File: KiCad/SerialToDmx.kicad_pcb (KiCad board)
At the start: 2 copper layers, 65 x 40 mm, 28 parts, among them U1 XIAO ESP32 C3, U2 TEA1-0505, U3 H11L1, U4 H11L1, U5 H11L1, U6 ST485EBDR, U7 H11L1

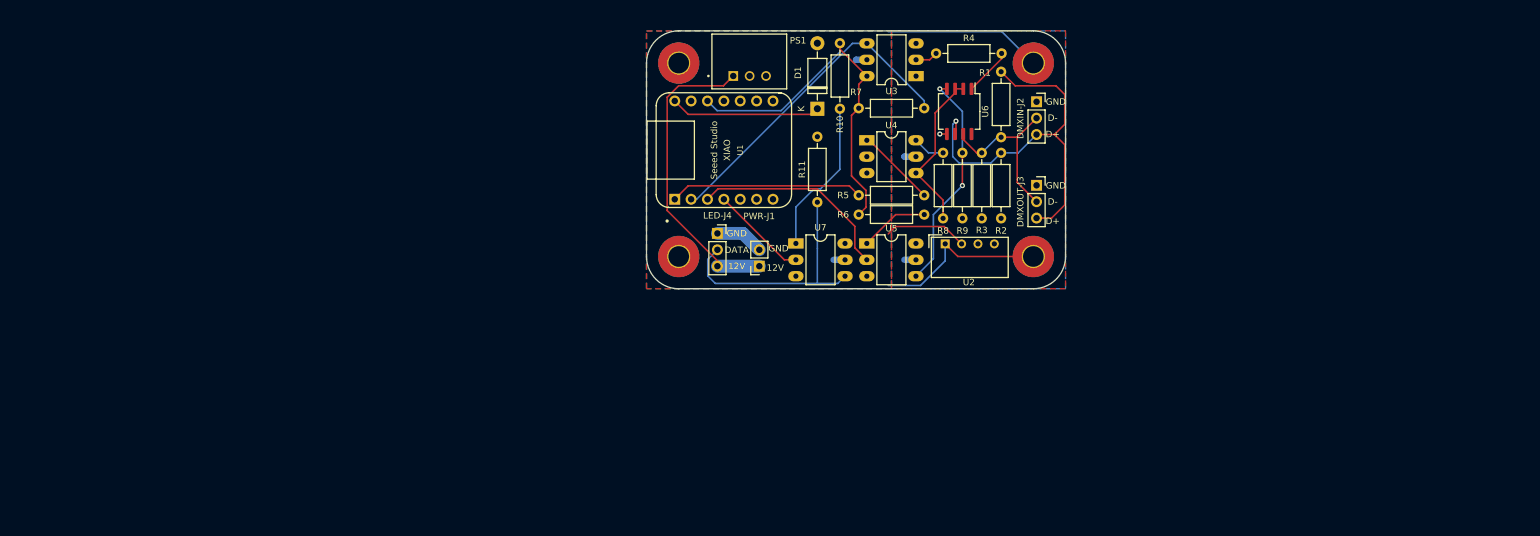
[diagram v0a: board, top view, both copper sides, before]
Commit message: Started Work on Conn Box V2
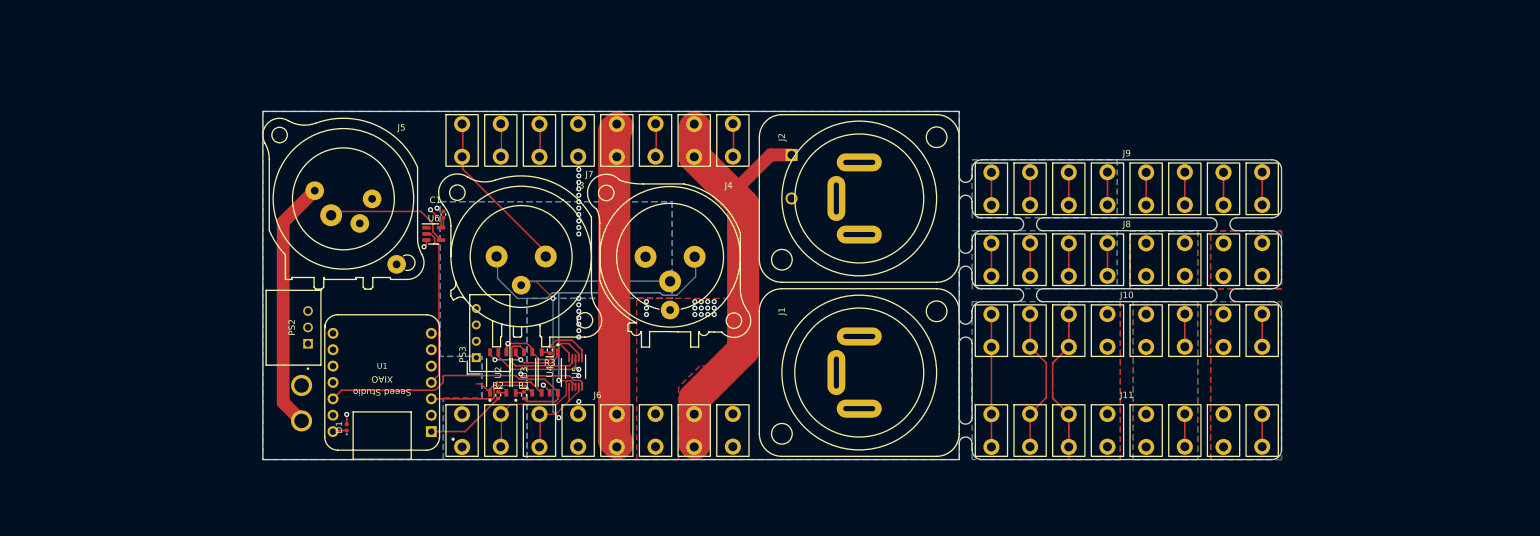
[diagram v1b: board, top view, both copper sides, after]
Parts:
- removed DMXIN-J2, DMXOUT-J3, LED-J4: Conn_01x03_Socket, Connector_PinSocket_2.54mm:PinSocket_1x03_P2.54mm_Vertical
- removed H1, H2, H3, H4: MountingHole_Pad, MountingHole:MountingHole_3.2mm_M3_Pad_TopBottom
- removed PWR-J1: Conn_01x02_Socket, Connector_PinSocket_2.54mm:PinSocket_1x02_P2.54mm_Vertical
- removed R10, R5, R6: 330R, Resistor_THT:R_Axial_DIN0207_L6.3mm_D2.5mm_P10.16mm_Horizontal
- removed R11, R4, R7, R8, R9: 470R, Resistor_THT:R_Axial_DIN0207_L6.3mm_D2.5mm_P10.16mm_Horizontal
- removed U7: H11L1, Package_DIP:DIP-6_W7.62mm_LongPads
- added C1: 0.1uC, Capacitor_SMD:C_0402_1005Metric, F.Cu at (118.5, 81.0)
- added J1: NAC3MPXXA, NeutrikCustom:NAC3MPXXA, F.Cu at (183.0, 105.5)
- added J10: Conn_01x08_Pin, Connector_Faston_Custom:Faston_01x08_pin, F.Cu at (203.5, 99.0)
- added J11: Conn_01x08_Pin, Connector_Faston_Custom:Faston_01x08_pin, F.Cu at (203.5, 114.5)
- added J2: NAC3MPXXB, NeutrikCustom:NAC3MPXXB, F.Cu at (183.0, 78.5)
- added J3: NC3FAV, NeutrikCustom:NC3FAV, F.Cu at (130.8, 86.5)
- added J4: NC3MAV, NeutrikCustom:NC3MAV, F.Cu at (153.8, 86.5)
- added J5: NC4FAV, NeutrikCustom:NC4FAV, F.Cu at (103.0, 77.5)
- added J6: Conn_01x08_Socket, Connector_Faston_Custom:Faston_01x08_socket, F.Cu at (121.4, 114.5)
- added J7: Conn_01x08_Socket, Connector_Faston_Custom:Faston_01x08_socket, F.Cu at (121.4, 69.5)
- added J8: Conn_01x08_Pin, Connector_Faston_Custom:Faston_01x08_pin, F.Cu at (203.5, 88.0)
- added J9: Conn_01x08_Pin, Connector_Faston_Custom:Faston_01x08_pin, F.Cu at (203.5, 77.0)
- added PS2: R-78E5.0-0.5, CONV_R-78E5.0-0.5:CONV_R-78E5.0-0.5, F.Cu at (95.2, 98.5)
- added PS3: TEA1-0505, Converter_DCDC:Converter_DCDC_TRACO_TEA1-xxxx_THT, F.Cu at (123.6, 103.2)
- D1: footprint Diode_THT:D_DO-41_SOD81_P10.16mm_Horizontal -> Diode_SMD:D_0402_1005Metric
- PS1: value R-78E5.0-0.5 -> IRM-45-12; footprint CONV_R-78E5.0-0.5:CONV_R-78E5.0-0.5 -> IRM-45-12:CONV_IRM-45-12; moved to B.Cu
- R1: value 120R -> 169R; footprint Resistor_THT:R_Axial_DIN0207_L6.3mm_D2.5mm_P10.16mm_Horizontal -> Resistor_SMD:R_0402_1005Metric
- R2: value 720R -> 169R; footprint Resistor_THT:R_Axial_DIN0207_L6.3mm_D2.5mm_P10.16mm_Horizontal -> Resistor_SMD:R_0402_1005Metric
- R3: value 720R -> 330R; footprint Resistor_THT:R_Axial_DIN0207_L6.3mm_D2.5mm_P10.16mm_Horizontal -> Resistor_SMD:R_0402_1005Metric
- U2: value TEA1-0505 -> ISOM8710DFFR; footprint Converter_DCDC:Converter_DCDC_TRACO_TEA1-xxxx_THT -> TICustom:ISOM8710
- U3, U4: value H11L1 -> ISOM8710DFFR; footprint Package_DIP:DIP-6_W7.62mm_LongPads -> TICustom:ISOM8710
- U5: value H11L1 -> THVD1512DGS; footprint Package_DIP:DIP-6_W7.62mm_LongPads -> TICustom:DGS0010A_N
- U6: value ST485EBDR -> SN74LV1T34DBV; footprint Package_SO:SO-8_5.3x6.2mm_P1.27mm -> Package_TO_SOT_SMD:SOT-23-5
- moved D1 88.2 mm to (103.5, 114.0)
- moved R1 84.1 mm to (131.0, 109.0)
- moved U6 83.7 mm to (117.0, 84.0), turned to 0 degrees
- moved R2 82.7 mm to (127.0, 109.0)
- moved U3 76.2 mm to (131.0, 105.5), turned to 90 degrees
- moved R3 73.6 mm to (135.0, 102.0), turned to 90 degrees
- moved U2 72.1 mm to (127.0, 105.5), turned to 90 degrees
- moved U1 64.1 mm to (109.0, 107.0), turned to 180 degrees
- moved U4 61.0 mm to (135.0, 105.5), turned to -90 degrees
- moved U5 49.4 mm to (139.0, 105.5), turned to -90 degrees
- moved PS1 47.6 mm to (134.3, 92.8), turned to 180 degrees
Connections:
- R1 pad 1: Net-(DMXIN-J2-Pin_2) -> 3V3
- R1 pad 2: Net-(DMXIN-J2-Pin_3) -> Net-(U3-AN)
- R2 pad 1: VCC_Iso -> DMX_DRIVE
- R2 pad 2: Net-(DMXIN-J2-Pin_3) -> Net-(U2-CAT)
- R3 pad 1: Net-(DMXIN-J2-Pin_2) -> Net-(U4-CAT)
- R3 pad 2: GND_Iso -> Net-(U5-R)
- U1 pad 1: DMX_READ -> DMX_DRIVE
- U1 pad 4: LED_DATA -> LED_DATA_33
- U2 pad 2: 5V -> Net-(U2-CAT)
- U2 pad 4: VCC_Iso -> Net-(U2-OUT)
- U3 pad 1: VCC_Iso -> Net-(U3-AN)
- U3 pad 2: Net-(R4-Pad1) -> DMX_TX
- U3 pad 3: unconnected-(U3-Pad3) -> GND_Iso
- U3 pad 4: DMX_RX -> Net-(U3-OUT)
- U3 pad 5: GND -> VCC_Iso
- U4 pad 1: Net-(R5-Pad2) -> VCC_Iso
- U4 pad 2: GND -> Net-(U4-CAT)
- U4 pad 3: unconnected-(U4-Pad3) -> GND
- U4 pad 4: Net-(U6-DE) -> DMX_RX
- U4 pad 5: GND_Iso -> 3V3
- U5 pad 1: Net-(R6-Pad2) -> Net-(U5-R)
- U5 pad 2: DMX_TX -> GND_Iso
- U5 pad 3: unconnected-(U5-Pad3) -> Net-(U2-OUT)
- U5 pad 4: Net-(U6-DI) -> Net-(U3-OUT)
- U5 pad 6: VCC_Iso -> DMX+
- U6 pad 1: Net-(U6-RO) -> unconnected-(U6-NC-Pad1)
- U6 pad 2: Net-(U6-DE) -> LED_DATA_33
- U6 pad 3: Net-(U6-DE) -> GND
- U6 pad 4: Net-(U6-DI) -> LED_DATA_50
- U6 pad 5: GND_Iso -> 5V
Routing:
- net N: track 0.00 -> 128.5 mm
- net L: track 0.00 -> 122.2 mm
- net DMX-: track 0.00 -> 97.5 mm, vias 0 -> 1
- net DMX+: track 0.00 -> 89.6 mm, vias 0 -> 2
- net Net-(DMXIN-J2-Pin_3): track 60.6 -> 0.00 mm, vias 1 -> 0
- net GND: track 63.1 -> 112.8 mm, vias 0 -> 23
- net GND_Iso: track 4.69 -> 46.4 mm
- net Net-(LED-J4-Pin_2): track 39.5 -> 0.00 mm
- net Net-(U6-DI): track 34.6 -> 0.00 mm, vias 2 -> 0
- net 12V: track 47.6 -> 81.9 mm
- net DMX_RX: track 51.0 -> 20.9 mm, vias 0 -> 1
- net DMX_READ: track 30.0 -> 0.00 mm
- net Net-(DMXIN-J2-Pin_2): track 26.0 -> 0.00 mm
- net Net-(U6-DE): track 25.0 -> 0.00 mm
- net LED_DATA_33: track 0.00 -> 24.8 mm
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- added copper zone on In2.Cu, net 5V
- added copper zone on B.Cu, net GND-Connection-Bridge
- added copper zone on F.Cu, net GND-Connection-Bridge
- added copper zone on In1.Cu, net GND-Connection-Bridge
- added copper zone on In2.Cu, net GND-Connection-Bridge
- added copper zone on B.Cu, net GND-Connection-In-Termination
- added copper zone on In1.Cu, net GND-Connection-In-Termination
- added copper zone on In2.Cu, net GND-Connection-In-Termination
- added copper zone on B.Cu, net GND-Connection-Out-Termination
- added copper zone on In1.Cu, net GND-Connection-Out-Termination
- added copper zone on In2.Cu, net GND-Connection-Out-Termination
- added copper zone on B.Cu, net L-Connection-Bridge
- added copper zone on F.Cu, net L-Connection-Bridge
- added copper zone on In1.Cu, net L-Connection-Bridge
- added copper zone on In2.Cu, net L-Connection-Bridge
- added copper zone on B.Cu, net L-Connection-Termination
- added copper zone on F.Cu, net L-Connection-Termination
- added copper zone on In1.Cu, net L-Connection-Termination
- added copper zone on In2.Cu, net L-Connection-Termination
- added copper zone on In2.Cu, net L-switched
- added copper zone on B.Cu, net N-Connection-Bridge
- added copper zone on F.Cu, net N-Connection-Bridge
- added copper zone on In1.Cu, net N-Connection-Bridge
- added copper zone on In2.Cu, net N-Connection-Bridge
- added copper zone on B.Cu, net N-Connection-Termination
- added copper zone on F.Cu, net N-Connection-Termination
- added copper zone on In1.Cu, net N-Connection-Termination
- added copper zone on In2.Cu, net N-Connection-Termination
- added copper zone on F.Cu, net N-switched
- added copper zone on In1.Cu, net N-switched
- added copper zone on In2.Cu, net N-switched
- added copper zone on In2.Cu, net VCC_Iso
- removed copper zone on F.Cu, net 5V
- removed copper zone on F.Cu, net VCC_Iso
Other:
- board size 65 x 40 mm -> 158 x 54 mm
- copper layers 2 -> 4

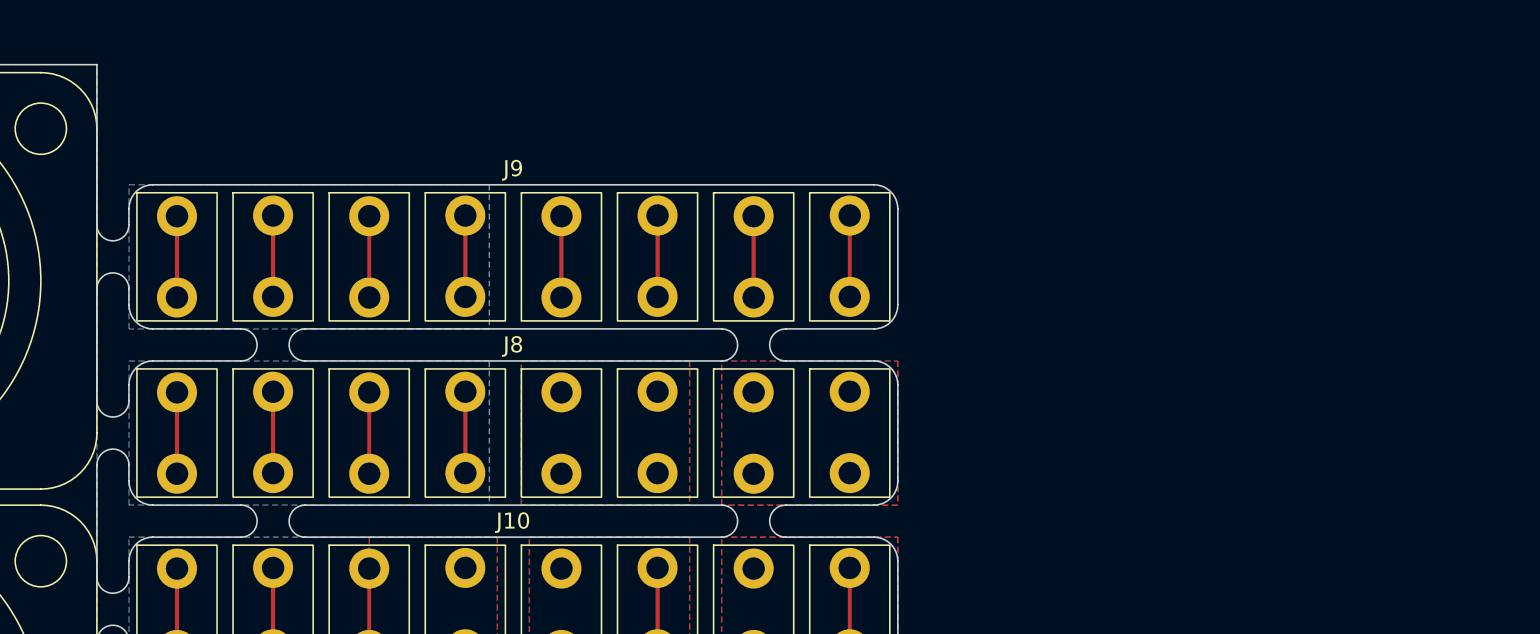
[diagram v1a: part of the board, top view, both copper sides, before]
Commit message: Started on Mounting Holes for Terminators and Bridge
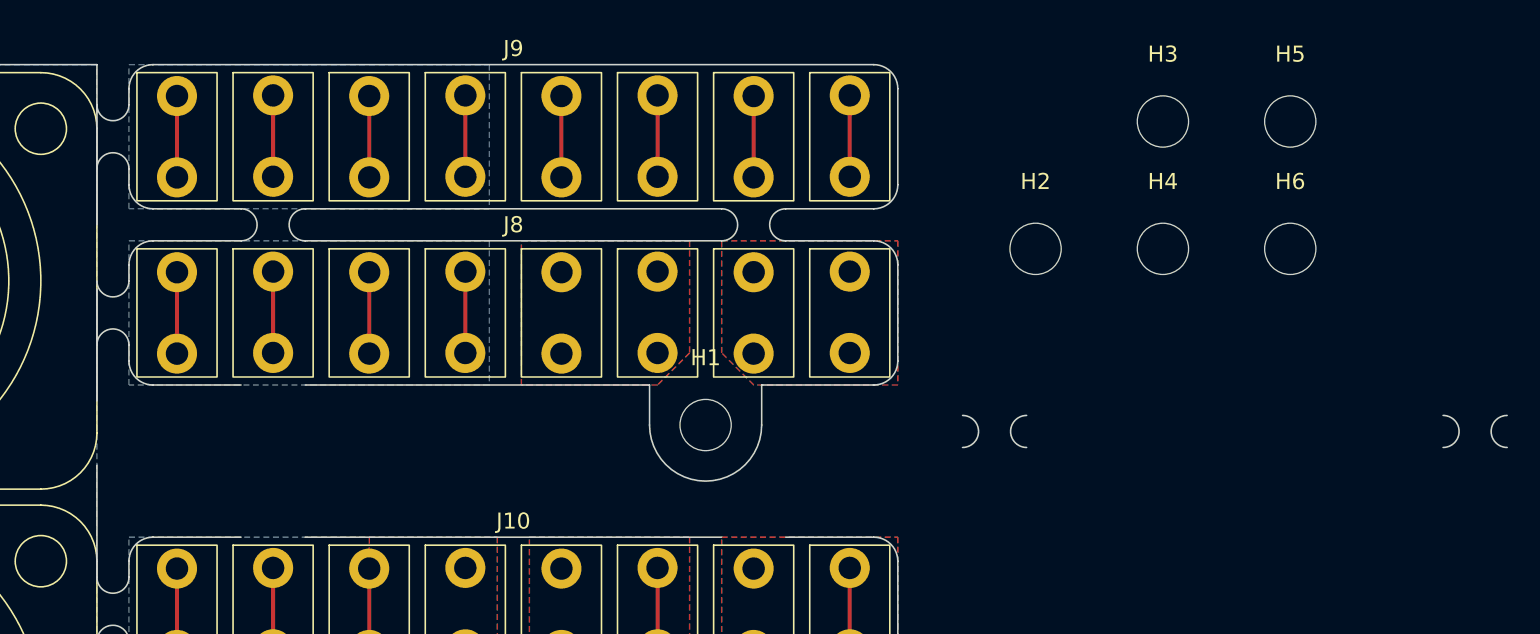
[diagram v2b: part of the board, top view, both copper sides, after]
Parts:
- added H1: MountingHole, MountingHole:MountingHole_3.2mm_M3, F.Cu at (236.5, 87.5)
- added H2: MountingHole, MountingHole:MountingHole_3.2mm_M3, F.Cu at (257.1, 76.5)
- added H3: MountingHole, MountingHole:MountingHole_3.2mm_M3, F.Cu at (265.1, 68.5)
- added H4: MountingHole, MountingHole:MountingHole_3.2mm_M3, F.Cu at (265.1, 76.5)
- added H5: MountingHole, MountingHole:MountingHole_3.2mm_M3, F.Cu at (273.0, 68.5)
- added H6: MountingHole, MountingHole:MountingHole_3.2mm_M3, F.Cu at (273.0, 76.5)
- moved J8 7.50 mm to (203.5, 80.5)
- moved J9 7.50 mm to (203.5, 69.5)
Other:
- board size 158 x 54 mm -> 196 x 54 mm

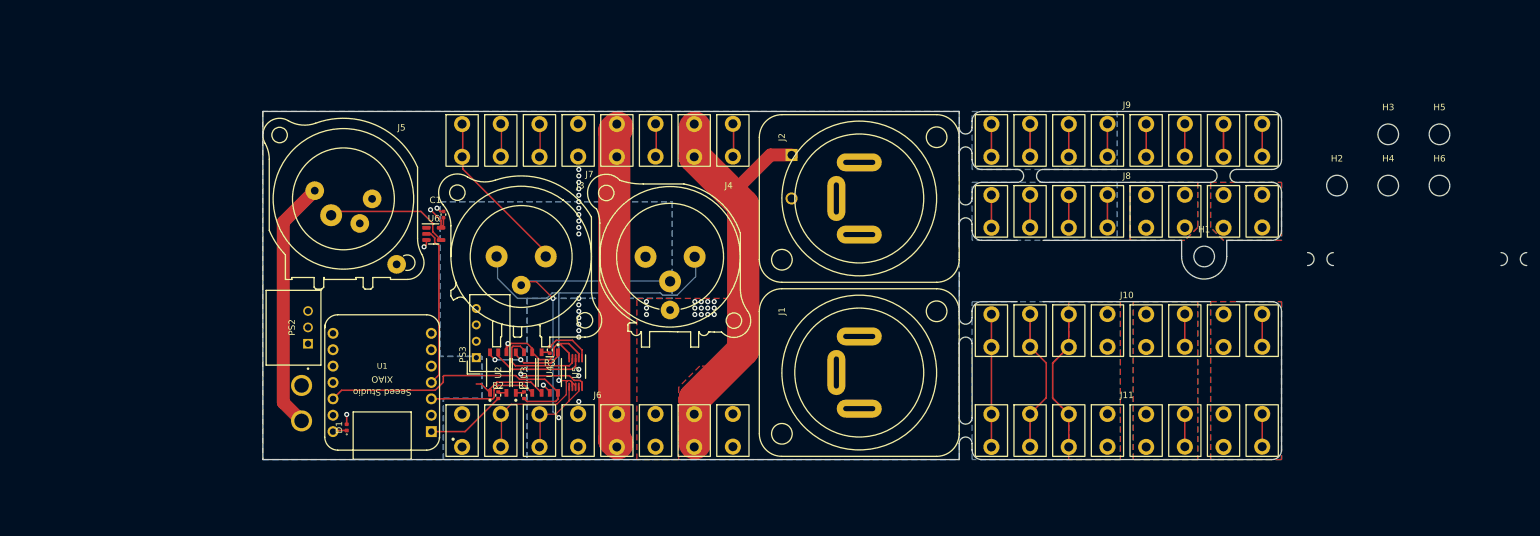
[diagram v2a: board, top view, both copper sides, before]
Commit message: Improved Layout for Case
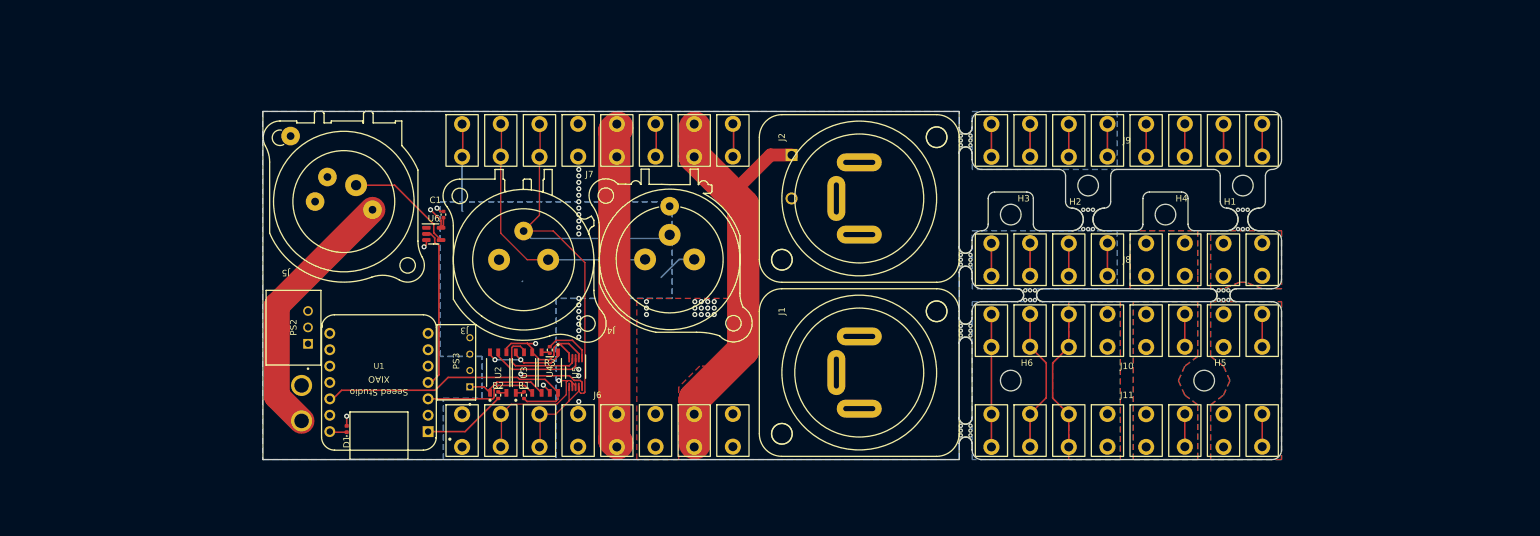
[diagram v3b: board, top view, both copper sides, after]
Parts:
- added H10: Mousebite, Panelization:mouse-bite-2mm-slot, F.Cu at (199.5, 88.0)
- added H11: Mousebite, Panelization:mouse-bite-2mm-slot, F.Cu at (199.5, 69.5)
- added H12: Mousebite, Panelization:mouse-bite-3.5mm-slot, F.Cu at (218.5, 81.8)
- added H13: Mousebite, Panelization:mouse-bite-3.5mm-slot, F.Cu at (242.5, 81.8)
- added H14: Mousebite, Panelization:mouse-bite-2mm-slot, F.Cu at (199.5, 114.5)
- added H7: Mousebite, Panelization:mouse-bite-2mm-slot, F.Cu at (239.5, 93.5)
- added H8: Mousebite, Panelization:mouse-bite-2mm-slot, F.Cu at (209.5, 93.5)
- added H9: Mousebite, Panelization:mouse-bite-2mm-slot, F.Cu at (199.5, 99.0)
- PS3: footprint Converter_DCDC:Converter_DCDC_TRACO_TEA1-xxxx_THT -> TracoCustom:CONV_TEA_1-0505
- moved H6 73.1 mm to (206.5, 106.8)
- moved H3 59.9 mm to (206.5, 81.0)
- moved H5 52.8 mm to (236.5, 106.8)
- moved H2 38.6 mm to (218.5, 76.5)
- moved H4 34.8 mm to (230.5, 81.0)
- moved H1 12.5 mm to (242.5, 76.5)
- moved J8 7.50 mm to (203.5, 88.0)
- moved J5 2.54 mm to (103.0, 80.0), turned to 180 degrees
- moved J4 2.51 mm to (153.5, 89.0), turned to 180 degrees
- moved J3 2.50 mm to (130.8, 89.0), turned to 180 degrees
- moved PS3 1.23 mm to (122.6, 103.9)
- moved U1 0.50 mm to (108.5, 107.0)
- moved D1 0.27 mm to (103.5, 114.3)
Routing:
- net DMX-: track 97.5 -> 84.2 mm
- net GND_Iso: track 46.4 -> 40.9 mm
- net 12V: track 81.9 -> 85.8 mm
- net LED_DATA_50: track 19.8 -> 17.5 mm
- net GND: track 112.8 -> 113.6 mm
- net 3V3: track 44.7 -> 43.9 mm
- net Net-(D1-K): track 2.20 -> 2.91 mm
- net DMX+: track 89.6 -> 89.8 mm, vias 2 -> 0
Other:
- board size 196 x 54 mm -> 158 x 54 mm
